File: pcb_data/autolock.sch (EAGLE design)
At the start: 20 parts, among them CN1 RASPBERRYPI-GPIO, T1 2SC1815

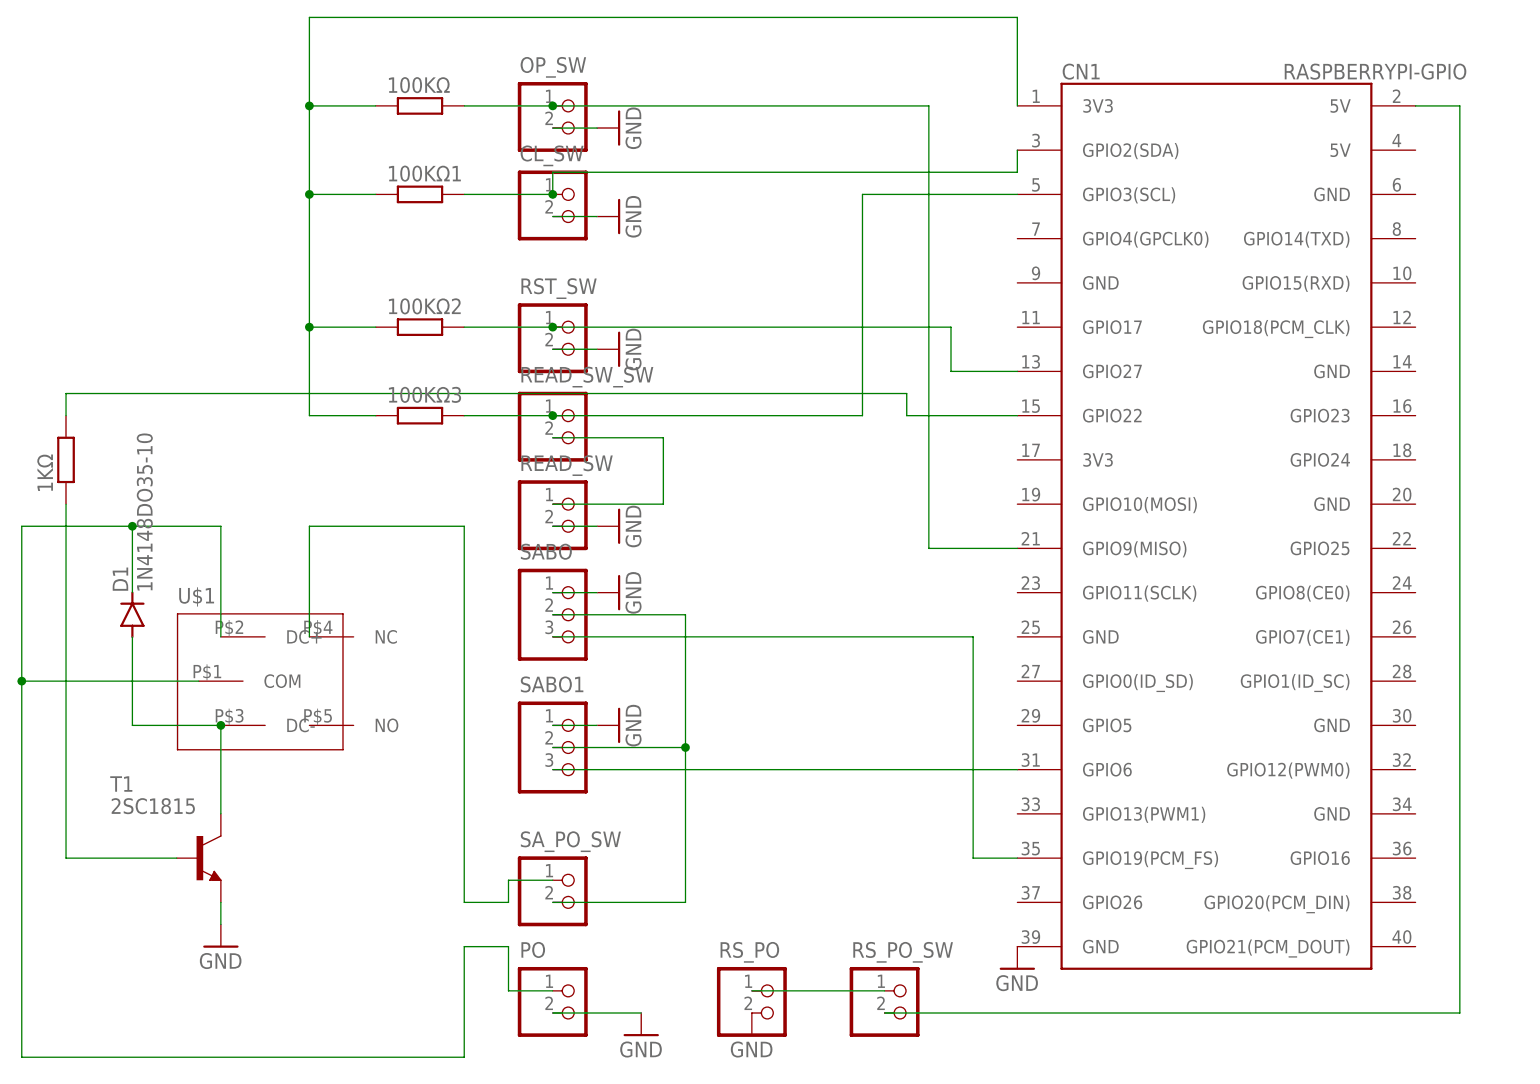
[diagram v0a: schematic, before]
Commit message: 基板GND周り修正、実装図追加
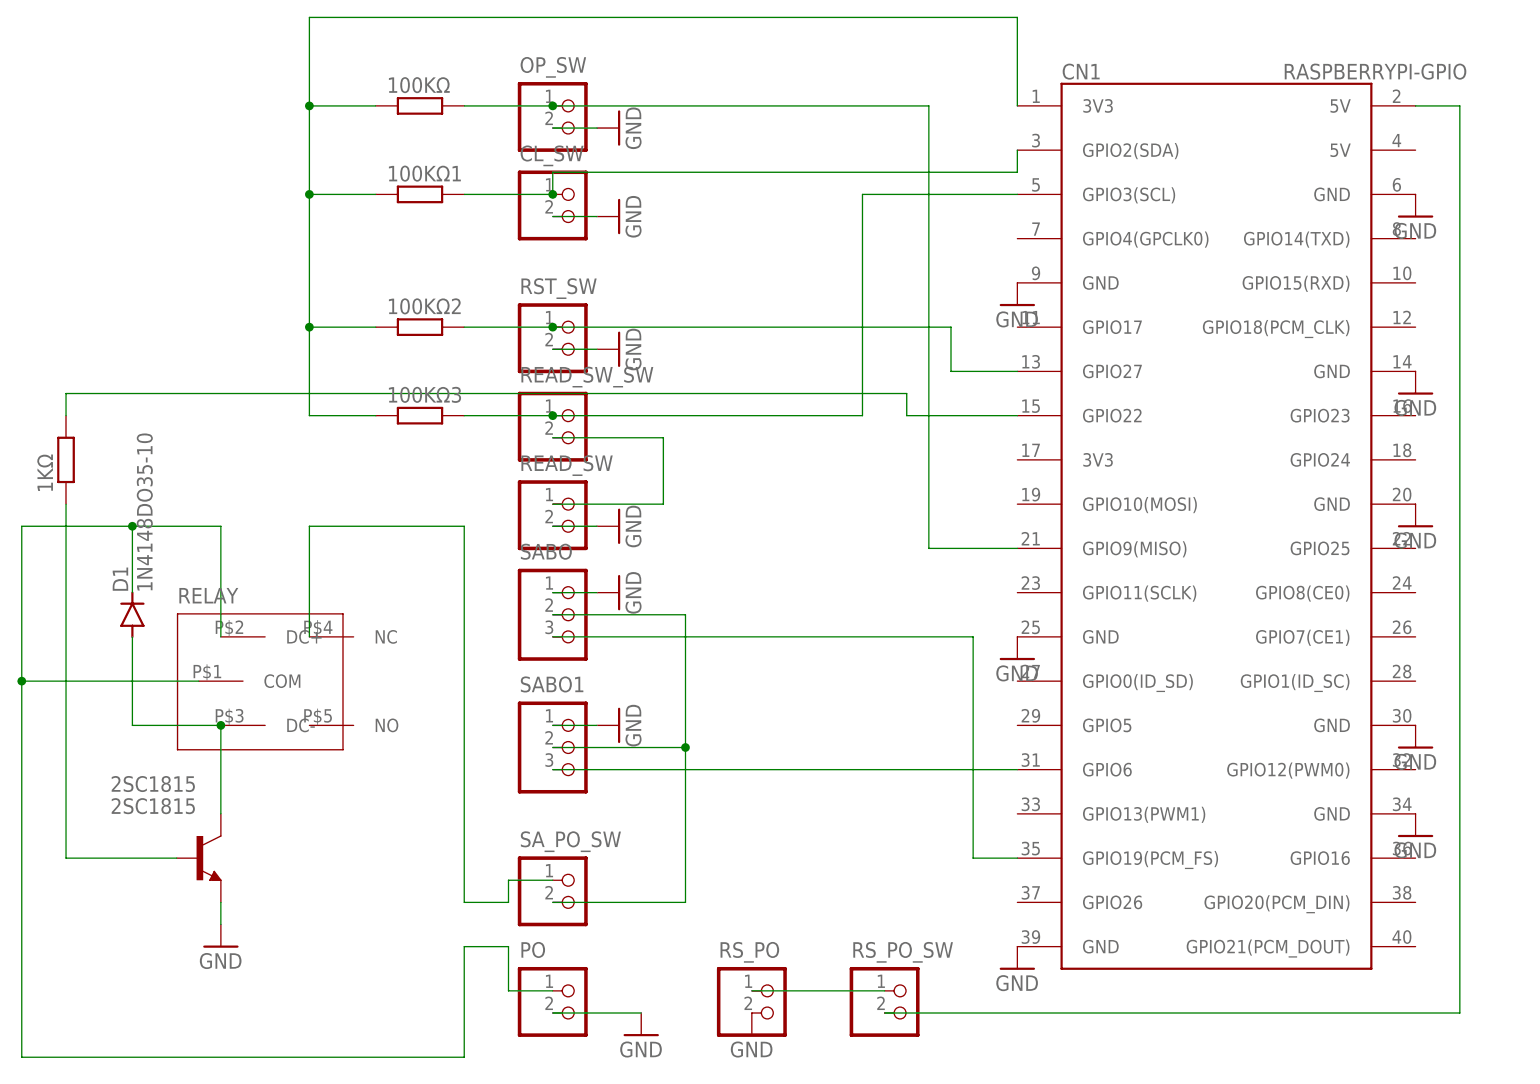
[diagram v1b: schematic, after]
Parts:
- renumbered T1 to 2SC1815, U$1 to RELAY
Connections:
- net GND: now also CN1.GND@1, CN1.GND@2, CN1.GND@3, CN1.GND@4, CN1.GND@5, CN1.GND@6, CN1.GND@7
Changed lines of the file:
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@@
 <part name="GND7" library="supply1" library_urn="urn:adsk.eagle:library:371" deviceset="GND" device=""/>
 <part name="GND8" library="supply1" library_urn="urn:adsk.eagle:library:371" deviceset="GND" device=""/>
-<part name="U$1" library="SRD05VDCSLC" deviceset="SRD05VDCSLC" device=""/>
-<part name="T1" library="transistor" library_urn="urn:adsk.eagle:library:402" deviceset="2SC1815" device="" package3d_urn="urn:adsk.eagle:package:29929/2"/>
+<part name="RELAY" library="SRD05VDCSLC" deviceset="SRD05VDCSLC" device=""/>
+<part name="2SC1815" library="transistor" library_urn="urn:adsk.eagle:library:402" deviceset="2SC1815" device="" package3d_urn="urn:adsk.eagle:package:29929/2"/>
 <part name="GND9" library="supply1" library_urn="urn:adsk.eagle:library:371" deviceset="GND" device=""/>
 <part name="100KΩ" library="rcl" library_urn="urn:adsk.eagle:library:334" deviceset="R-EU_" device="0207/10" package3d_urn="urn:adsk.eagle:package:23491/2"/>
@@
 <part name="D1" library="diode" library_urn="urn:adsk.eagle:library:210" deviceset="1N4148" device="DO35-10" package3d_urn="urn:adsk.eagle:package:43344/2"/>
 <part name="RS_PO_SW" library="jst-xh" deviceset="B2B-XH-A" device="" package3d_urn="urn:adsk.eagle:package:36017608/1"/>
+<part name="GND11" library="supply1" library_urn="urn:adsk.eagle:library:371" deviceset="GND" device=""/>
+<part name="GND12" library="supply1" library_urn="urn:adsk.eagle:library:371" deviceset="GND" device=""/>
+<part name="GND13" library="supply1" library_urn="urn:adsk.eagle:library:371" deviceset="GND" device=""/>
+<part name="GND14" library="supply1" library_urn="urn:adsk.eagle:library:371" deviceset="GND" device=""/>
+<part name="GND15" library="supply1" library_urn="urn:adsk.eagle:library:371" deviceset="GND" device=""/>
+<part name="GND16" library="supply1" library_urn="urn:adsk.eagle:library:371" deviceset="GND" device=""/>
+<part name="GND17" library="supply1" library_urn="urn:adsk.eagle:library:371" deviceset="GND" device=""/>
 </parts>
 <sheets>
@@
 <attribute name="VALUE" x="40.64" y="63.5" size="1.778" layer="96" rot="R90"/>
 </instance>
-<instance part="U$1" gate="G$1" x="-12.7" y="35.56" smashed="yes">
+<instance part="RELAY" gate="G$1" x="-12.7" y="35.56" smashed="yes">
 <attribute name="NAME" x="-12.6" y="36.86" size="1.778" layer="95"/>
 </instance>
-<instance part="T1" gate="G$1" x="-10.16" y="7.62" smashed="yes">
+<instance part="2SC1815" gate="G$1" x="-10.16" y="7.62" smashed="yes">
 <attribute name="NAME" x="-20.32" y="15.24" size="1.778" layer="95"/>
 <attribute name="VALUE" x="-20.32" y="12.7" size="1.778" layer="96"/>
@@
 <attribute name="NAME" x="64.77" y="-3.81" size="1.778" layer="95"/>
 <attribute name="VALUE" x="64.77" y="-15.24" size="1.778" layer="96"/>
+</instance>
+<instance part="GND11" gate="1" x="83.82" y="30.48" smashed="yes">
+<attribute name="VALUE" x="81.28" y="27.94" size="1.778" layer="96"/>
+</instance>
+<instance part="GND12" gate="1" x="83.82" y="71.12" smashed="yes">
+<attribute name="VALUE" x="81.28" y="68.58" size="1.778" layer="96"/>
+</instance>
+<instance part="GND13" gate="1" x="129.54" y="81.28" smashed="yes">
+<attribute name="VALUE" x="127" y="78.74" size="1.778" layer="96"/>
+</instance>
+<instance part="GND14" gate="1" x="129.54" y="60.96" smashed="yes">
+<attribute name="VALUE" x="127" y="58.42" size="1.778" layer="96"/>
+</instance>
+<instance part="GND15" gate="1" x="129.54" y="45.72" smashed="yes">
+<attribute name="VALUE" x="127" y="43.18" size="1.778" layer="96"/>
+</instance>
+<instance part="GND16" gate="1" x="129.54" y="20.32" smashed="yes">
+<attribute name="VALUE" x="127" y="17.78" size="1.778" layer="96"/>
+</instance>
+<instance part="GND17" gate="1" x="129.54" y="10.16" smashed="yes">
+<attribute name="VALUE" x="127" y="7.62" size="1.778" layer="96"/>
 </instance>
 </instances>
@@
 <segment>
 <pinref part="GND9" gate="1" pin="GND"/>
-<pinref part="T1" gate="G$1" pin="E"/>
+<pinref part="2SC1815" gate="G$1" pin="E"/>
 <wire x1="-7.62" y1="0" x2="-7.62" y2="2.54" width="0.1524" layer="91"/>
+</segment>
+<segment>
+<pinref part="CN1" gate="G$1" pin="GND@5"/>
+<pinref part="GND11" gate="1" pin="GND"/>
+</segment>
+<segment>
+<pinref part="CN1" gate="G$1" pin="GND@2"/>
+<pinref part="GND12" gate="1" pin="GND"/>
+</segment>
+<segment>
+<pinref part="CN1" gate="G$1" pin="GND@1"/>
+<pinref part="GND13" gate="1" pin="GND"/>
+</segment>
+<segment>
+<pinref part="CN1" gate="G$1" pin="GND@3"/>
+<pinref part="GND14" gate="1" pin="GND"/>
+</segment>
+<segment>
+<pinref part="CN1" gate="G$1" pin="GND@4"/>
+<pinref part="GND15" gate="1" pin="GND"/>
+</segment>
+<segment>
+<pinref part="CN1" gate="G$1" pin="GND@6"/>
+<pinref part="GND16" gate="1" pin="GND"/>
+</segment>
+<segment>
+<pinref part="CN1" gate="G$1" pin="GND@7"/>
+<pinref part="GND17" gate="1" pin="GND"/>
 </segment>
 </net>
@@
 <wire x1="20.32" y1="2.54" x2="25.4" y2="2.54" width="0.1524" layer="91"/>
 <wire x1="20.32" y1="45.72" x2="20.32" y2="2.54" width="0.1524" layer="91"/>
-<pinref part="U$1" gate="G$1" pin="NC"/>
+<pinref part="RELAY" gate="G$1" pin="NC"/>
 <wire x1="2.54" y1="33.02" x2="2.54" y2="45.72" width="0.1524" layer="91"/>
 <wire x1="2.54" y1="45.72" x2="20.32" y2="45.72" width="0.1524" layer="91"/>
@@
 <wire x1="-30.48" y1="27.94" x2="-30.48" y2="45.72" width="0.1524" layer="91"/>
 <wire x1="-7.62" y1="45.72" x2="-17.78" y2="45.72" width="0.1524" layer="91"/>
-<pinref part="U$1" gate="G$1" pin="DC+"/>
+<pinref part="RELAY" gate="G$1" pin="DC+"/>
 <wire x1="-17.78" y1="45.72" x2="-30.48" y2="45.72" width="0.1524" layer="91"/>
 <wire x1="-7.62" y1="45.72" x2="-7.62" y2="33.02" width="0.1524" layer="91"/>
-<pinref part="U$1" gate="G$1" pin="COM"/>
+<pinref part="RELAY" gate="G$1" pin="COM"/>
 <wire x1="-10.16" y1="27.94" x2="-30.48" y2="27.94" width="0.1524" layer="91"/>
 <junction x="-30.48" y="27.94"/>
@@
 <pinref part="1KΩ" gate="G$1" pin="1"/>
 <wire x1="-25.4" y1="48.26" x2="-25.4" y2="7.62" width="0.1524" layer="91"/>
-<pinref part="T1" gate="G$1" pin="B"/>
+<pinref part="2SC1815" gate="G$1" pin="B"/>
 <wire x1="-12.7" y1="7.62" x2="-25.4" y2="7.62" width="0.1524" layer="91"/>
 </segment>
@@
 <net name="N$1" class="0">
 <segment>
-<pinref part="U$1" gate="G$1" pin="DC-"/>
-<pinref part="T1" gate="G$1" pin="C"/>
+<pinref part="RELAY" gate="G$1" pin="DC-"/>
+<pinref part="2SC1815" gate="G$1" pin="C"/>
 <wire x1="-7.62" y1="22.86" x2="-7.62" y2="12.7" width="0.1524" layer="91"/>
 <pinref part="D1" gate="G$1" pin="A"/>
